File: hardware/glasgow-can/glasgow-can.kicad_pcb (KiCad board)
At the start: 2 copper layers, 34 parts, among them J1 Conn_02x10_Odd_Even, J2 A-DS 09 A/KG-T2S, J3 Conn_01x09_Male, J4 Conn_01x03_Male, J5 Conn_02x10_Odd_Even, J6 Conn_01x03, J7 Conn_01x02_Male, J8 Conn_01x02_Male, Q1 TLP240A, Q2 NX7002BKW, Q3 TLP240A, Q4 NX7002BKW, U1 TCAN1051, U2 TCAN1051

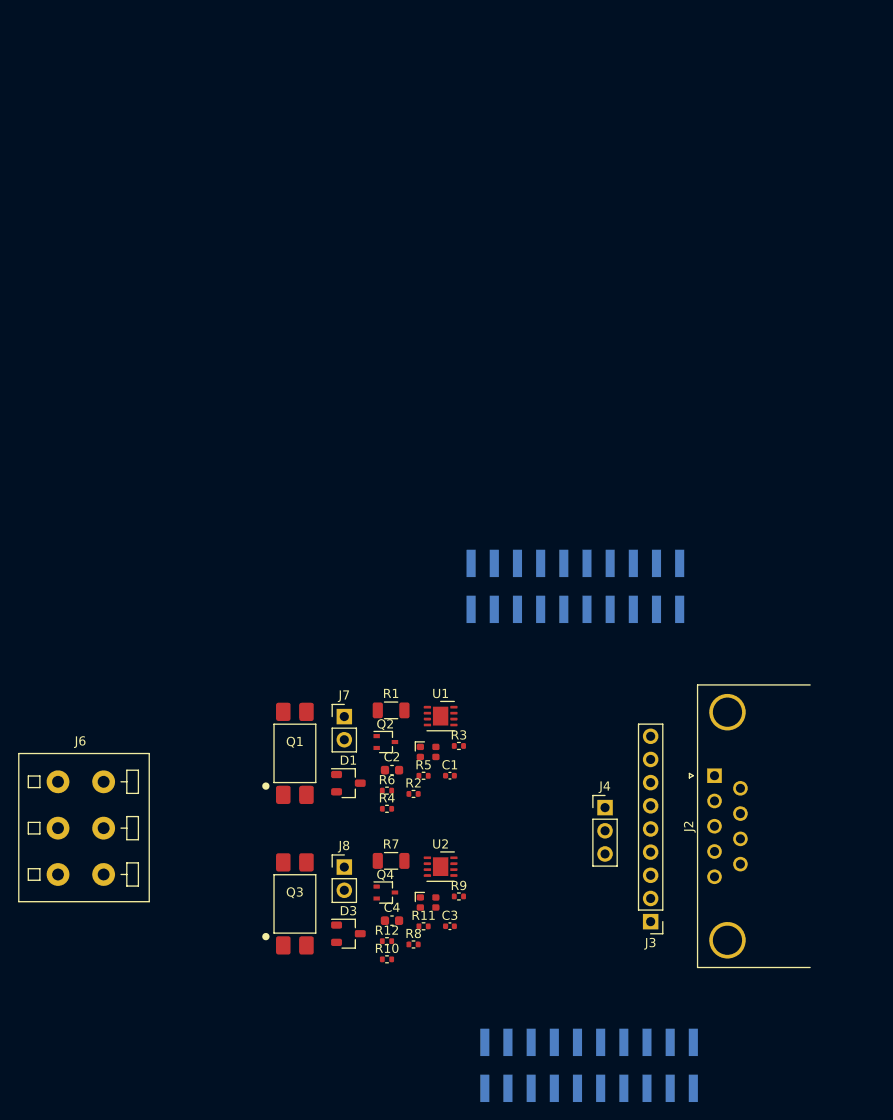
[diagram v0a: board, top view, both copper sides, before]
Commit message: schematic revised according to discussion in #1, and layout mostly complete... some TODOs remain
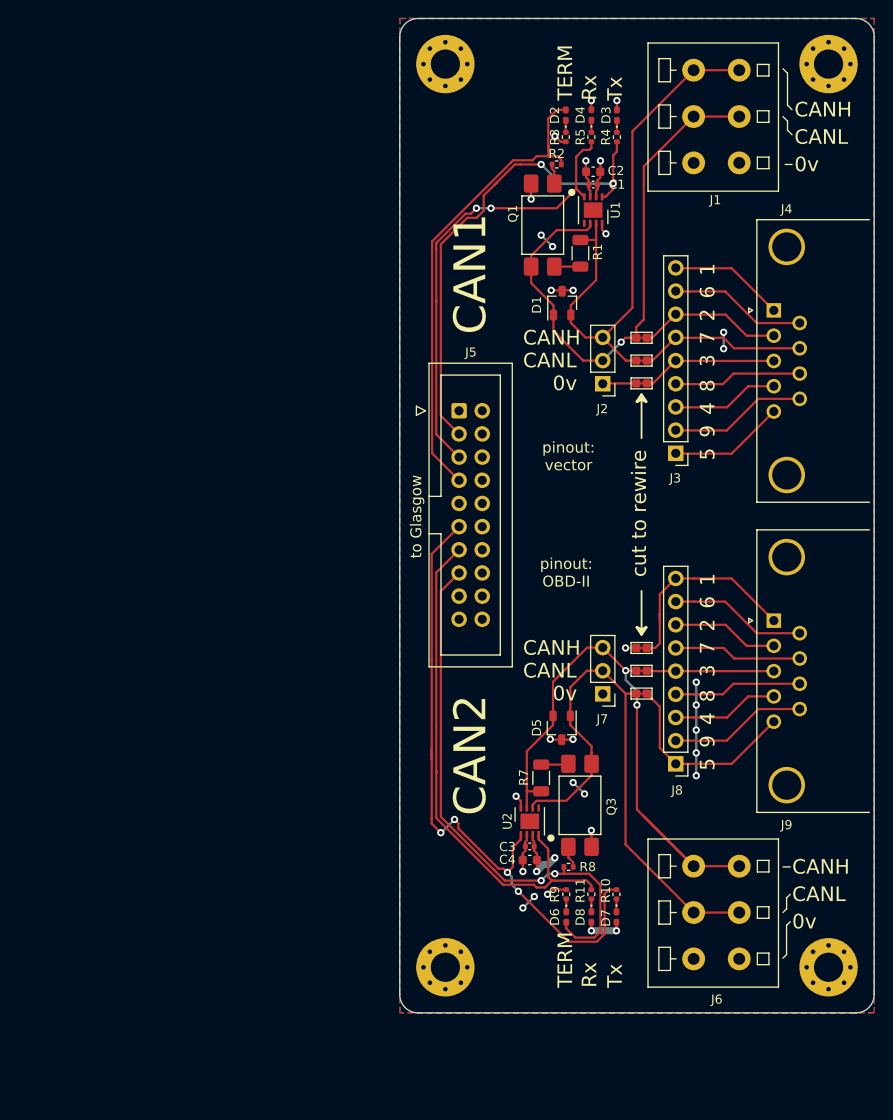
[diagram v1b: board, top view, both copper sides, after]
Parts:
- removed Q2, Q4: NX7002BKW, Package_TO_SOT_SMD:SOT-323_SC-70
- removed R12, R6: 25k, Resistor_SMD:R_0402_1005Metric
- added D5: PESD2CAN, rhais_package-smd:SOT-23, F.Cu at (171.8, 90.8)
- added D6: TJ-S1005SW4TGLC0A-A5, LED_SMD:LED_0402_1005Metric_Pad0.77x0.64mm_HandSolder, F.Cu at (172.2, 111.5)
- added D7: TJ-S1005SW4TGLC2G-A5, LED_SMD:LED_0402_1005Metric_Pad0.77x0.64mm_HandSolder, F.Cu at (177.8, 111.5)
- added D8: TJ-S1005SW4TGLC0A-A5, LED_SMD:LED_0402_1005Metric_Pad0.77x0.64mm_HandSolder, F.Cu at (175.0, 111.5)
- added H1: MountingHole_Pad, MountingHole:MountingHole_3.2mm_M3_Pad_Via, F.Cu at (159.0, 18.0)
- added H2: MountingHole_Pad, MountingHole:MountingHole_3.2mm_M3_Pad_Via, F.Cu at (201.0, 18.0)
- added H3: MountingHole_Pad, MountingHole:MountingHole_3.2mm_M3_Pad_Via, F.Cu at (159.0, 117.0)
- added H4: MountingHole_Pad, MountingHole:MountingHole_3.2mm_M3_Pad_Via, F.Cu at (201.0, 117.0)
- added J10: pkl_jumper_nc, pkl_jumpers:J_NC_0603_20, F.Cu at (180.5, 50.5)
- added J11: pkl_jumper_nc, pkl_jumpers:J_NC_0603_20, F.Cu at (180.5, 48.0)
- added J12: pkl_jumper_nc, pkl_jumpers:J_NC_0603_20, F.Cu at (180.5, 53.0)
- added J13: pkl_jumper_nc, pkl_jumpers:J_NC_0603_20, F.Cu at (180.5, 84.5)
- added J14: pkl_jumper_nc, pkl_jumpers:J_NC_0603_20, F.Cu at (180.5, 87.0)
- added J15: pkl_jumper_nc, pkl_jumpers:J_NC_0603_20, F.Cu at (180.5, 82.0)
- added J9: A-DS 09 A/KG-T2S, Connector_Dsub:DSUB-9_Female_Horizontal_P2.77x2.84mm_EdgePinOffset7.70mm_Housed_MountingHolesOffset9.12mm, F.Cu at (195.0, 79.0)
- D2, D4: value FM-B2020RGBA-HG -> TJ-S1005SW4TGLC0A-A5; footprint pkl_led:LED_TRI_2020 -> LED_SMD:LED_0402_1005Metric_Pad0.77x0.64mm_HandSolder
- D3: value PESD2CAN -> TJ-S1005SW4TGLC2G-A5; footprint rhais_package-smd:SOT-23 -> LED_SMD:LED_0402_1005Metric_Pad0.77x0.64mm_HandSolder
- J1: value Conn_02x10_Odd_Even -> 2834077-2; footprint Connector_PinSocket_2.54mm:PinSocket_2x10_P2.54mm_Vertical_SMD -> glasgow-can:TE_2834077-2; moved to F.Cu
- J2: value A-DS 09 A/KG-T2S -> Conn_01x03_Male; footprint Connector_Dsub:DSUB-9_Female_Horizontal_P2.77x2.84mm_EdgePinOffset7.70mm_Housed_MountingHolesOffset9.12mm -> Connector_PinHeader_2.54mm:PinHeader_1x03_P2.54mm_Vertical
- J4: value Conn_01x03_Male -> A-DS 09 A/KG-T2S; footprint Connector_PinHeader_2.54mm:PinHeader_1x03_P2.54mm_Vertical -> Connector_Dsub:DSUB-9_Female_Horizontal_P2.77x2.84mm_EdgePinOffset7.70mm_Housed_MountingHolesOffset9.12mm
- J5: footprint Connector_PinSocket_2.54mm:PinSocket_2x10_P2.54mm_Vertical_SMD -> Connector_IDC:IDC-Header_2x10_P2.54mm_Vertical; moved to F.Cu
- J6: value Conn_01x03 -> 2834077-2
- J7: value Conn_01x02_Male -> Conn_01x03_Male; footprint Connector_PinHeader_2.54mm:PinHeader_1x02_P2.54mm_Vertical -> Connector_PinHeader_2.54mm:PinHeader_1x03_P2.54mm_Vertical
- J8: value Conn_01x02_Male -> Conn_01x09_Male; footprint Connector_PinHeader_2.54mm:PinHeader_1x02_P2.54mm_Vertical -> Connector_PinHeader_2.54mm:PinHeader_1x09_P2.54mm_Vertical
- moved D3 94.4 mm to (177.8, 23.6), turned to 90 degrees
- moved D4 88.2 mm to (175.0, 23.6), turned to 90 degrees
- moved R4 77.8 mm to (177.8, 26.0), turned to 270 degrees
- moved J5 73.2 mm to (160.5, 56.0), turned to 0 degrees
- moved R5 72.4 mm to (175.0, 26.0), turned to 270 degrees
- moved D2 71.4 mm to (172.2, 23.6), turned to 90 degrees
- moved R2 70.8 mm to (171.2, 29.0)
- moved J6 70.4 mm to (188.8, 111.0), turned to 90 degrees
- moved C2 69.2 mm to (175.2, 29.8)
- moved R3 67.8 mm to (172.2, 26.0), turned to 270 degrees
- moved C1 66.7 mm to (175.2, 31.2)
- moved Q1 64.0 mm to (169.7, 35.6), turned to 180 degrees
- moved U1 57.9 mm to (175.2, 34.0), turned to 270 degrees
- moved D1 57.6 mm to (171.8, 44.2), turned to 90 degrees
- moved J4 57.6 mm to (195.0, 45.0), turned to 90 degrees
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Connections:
- C1 pad 1: /CAN1_+5V -> /+5V
- C2 pad 1: /CAN1_+5V -> /+5V
- C3 pad 1: /CAN2_+5V -> /+5V
- C4 pad 1: /CAN2_+5V -> /+5V
- D1 pad 1: /CAN1_H -> /CAN1_L
- D1 pad 2: /CAN1_L -> /CAN1_H
- D2 pad 2: Net-(D2-Pad2) -> /CAN1_TERM
- D3 pad 1: /CAN2_H -> Net-(D3-Pad1)
- D3 pad 2: /CAN2_L -> /+5V
- D4 pad 2: Net-(D4-Pad2) -> /+5V
- J1 pad 1: Net-(J1-Pad1) -> 0V
- J1 pad 2: /CAN1_+5V -> /CAN1_L
- J1 pad 3: /CAN1_TxD -> /CAN1_H
- J1 pad 5: /CAN1_RxD -> /CAN1_L
- J1 pad 6: 0V -> /CAN1_H
- J2 pad 1: Net-(J2-Pad1) -> 0V
- J2 pad 2: Net-(J2-Pad2) -> /CAN1_L
- J2 pad 3: Net-(J2-Pad3) -> /CAN1_H
- J3 pad 1: Net-(J2-Pad5) -> Net-(J3-Pad1)
- J3 pad 2: Net-(J2-Pad9) -> Net-(J3-Pad2)
- J3 pad 3: Net-(J2-Pad4) -> Net-(J3-Pad3)
- J3 pad 4: Net-(J2-Pad8) -> Net-(J3-Pad4)
- J3 pad 5: Net-(J2-Pad3) -> Net-(J12-Pad2)
- J3 pad 6: Net-(J2-Pad7) -> Net-(J10-Pad2)
- J3 pad 7: Net-(J2-Pad2) -> Net-(J11-Pad2)
- J3 pad 8: Net-(J2-Pad6) -> Net-(J3-Pad8)
- J3 pad 9: Net-(J2-Pad1) -> Net-(J3-Pad9)
- J4 pad 1: /CAN1_H -> Net-(J3-Pad9)
- J4 pad 2: /CAN1_L -> Net-(J11-Pad2)
- J4 pad 3: 0V -> Net-(J12-Pad2)
- J5 pad 11: /CAN2_TxLED -> /CAN2_TxD
- J5 pad 13: /CAN2_RxLED -> /CAN2_RxD
- J5 pad 15: Net-(J5-Pad15) -> /CAN2_TERM
- J5 pad 2: /CAN2_+5V -> /+5V
- J5 pad 3: /CAN2_TxD -> /CAN1_TxD
- J5 pad 5: /CAN2_RxD -> /CAN1_RxD
- J5 pad 7: /CAN2_S -> /CAN1_TERM
- J5 pad 9: /CAN2_TERM -> Net-(J5-Pad9)
- J6 pad 4: (no net) -> 0V
- J6 pad 5: (no net) -> /CAN2_L
- J6 pad 6: (no net) -> /CAN2_H
- J7 pad 1: /CAN1_L -> 0V
- J7 pad 2: 0V -> /CAN2_L
- J8 pad 1: /CAN2_L -> Net-(J14-Pad2)
- J8 pad 2: 0V -> Net-(J8-Pad2)
- R10 pad 1: Net-(D4-Pad4) -> Net-(D7-Pad1)
- R10 pad 2: /CAN2_TxLED -> /CAN2_TxD
- R11 pad 1: Net-(D4-Pad2) -> Net-(D8-Pad1)
- R11 pad 2: /CAN2_RxLED -> /CAN2_RxD
- R3 pad 2: Net-(Q2-Pad3) -> 0V
- R4 pad 1: Net-(D2-Pad4) -> Net-(D3-Pad1)
- R4 pad 2: /CAN1_TxLED -> /CAN1_TxD
- R5 pad 1: Net-(D2-Pad2) -> Net-(D4-Pad1)
- R5 pad 2: /CAN1_RxLED -> /CAN1_RxD
- R9 pad 1: Net-(D4-Pad1) -> Net-(D6-Pad1)
- R9 pad 2: Net-(Q4-Pad3) -> 0V
- U1 pad 3: /CAN1_+5V -> /+5V
- U1 pad 8: /CAN1_S -> 0V
- U2 pad 3: /CAN2_+5V -> /+5V
- U2 pad 8: /CAN2_S -> 0V
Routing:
- net /CAN2_TxD: track 0.00 -> 72.5 mm, vias 0 -> 4
- net /CAN2_H: track 0.00 -> 65.6 mm, vias 0 -> 2
- net /CAN1_H: track 0.00 -> 61.1 mm
- net /CAN1_L: track 0.00 -> 60.8 mm, vias 0 -> 1
- net /CAN2_L: track 0.00 -> 60.2 mm
- net /CAN2_TERM: track 0.00 -> 60.1 mm, vias 0 -> 2
- net /CAN2_RxD: track 0.00 -> 57.5 mm
- net /CAN1_TxD: track 0.00 -> 53.2 mm, vias 0 -> 2
- net /CAN1_TERM: track 0.00 -> 53.1 mm
- net /CAN1_RxD: track 0.00 -> 49.9 mm, vias 0 -> 2
- net /+5V: track 0.00 -> 35.0 mm, vias 0 -> 20
- net 0V: track 0.00 -> 29.1 mm, vias 0 -> 13
- net Net-(J15-Pad2): track 0.00 -> 22.9 mm
- net Net-(J14-Pad2): track 0.00 -> 21.7 mm
- net Net-(J10-Pad2): track 0.00 -> 18.3 mm
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- added copper zone on F.Cu, net /+5V
- added copper zone on B.Cu, net 0V
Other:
- board outline added: 52 x 109 mm
- board text added: "(0v)"
- board text added: "(Hi)"
- board text added: "(Lo)"
- board text added: "0v"
- board text added: "1"
- board text added: "2"
- board text added: "3"
- board text added: "4"
- board text added: "5"
- board text added: "6"
- board text added: "7"
- board text added: "8"
- board text added: "9"
- board text added: "CAN1"
- board text added: "CAN2"
- board text added: "CANH"
- board text added: "CANL"
- board text added: "Glasgow 2x CAN Add-On"
- board text added: "Rx"
- board text added: "TERM"
- board text added: "Tx"
- board text added: "cut to rewire"
- board text added: "default pinout: OBD-II cable"
- board text added: "default pinout: bosch / vector"
- board text added: "designed by: Attie Grande"
- board text added: "pinout: OBD-II"
- board text added: "pinout: vector"
- board text added: "to Glasgow"

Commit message: fix DE-9 footprint, spruce up schematic and layout
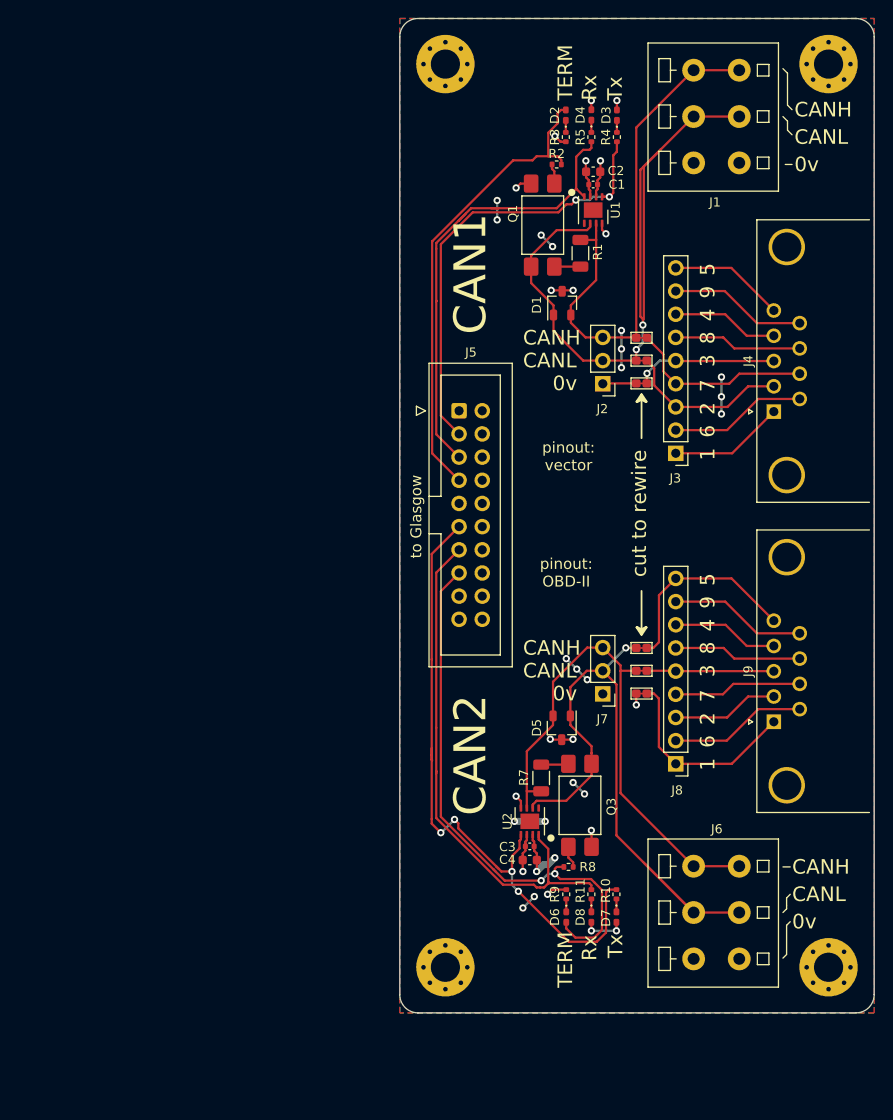
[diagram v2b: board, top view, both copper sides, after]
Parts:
- J4, J9: footprint Connector_Dsub:DSUB-9_Female_Horizontal_P2.77x2.84mm_EdgePinOffset7.70mm_Housed_MountingHolesOffset9.12mm -> Connector_Dsub:DSUB-9_Male_Horizontal_P2.77x2.84mm_EdgePinOffset7.70mm_Housed_MountingHolesOffset9.12mm
- moved J4 11.1 mm to (195.0, 56.1)
- moved J9 11.1 mm to (195.0, 90.1)
- moved J14 5.00 mm to (180.5, 82.0)
- moved J15 5.00 mm to (180.5, 87.0)
- moved J10 2.50 mm to (180.5, 48.0)
- moved J11 2.50 mm to (180.5, 50.5)
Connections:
- J3 pad 3: Net-(J3-Pad3) -> Net-(J11-Pad2)
- J3 pad 4: Net-(J3-Pad4) -> Net-(J10-Pad2)
- J3 pad 6: Net-(J10-Pad2) -> Net-(J3-Pad6)
- J3 pad 7: Net-(J11-Pad2) -> Net-(J3-Pad7)
- J4 pad 1: Net-(J3-Pad9) -> Net-(J3-Pad1)
- J4 pad 4: Net-(J3-Pad3) -> Net-(J3-Pad7)
- J4 pad 5: Net-(J3-Pad1) -> Net-(J3-Pad9)
- J4 pad 6: Net-(J3-Pad8) -> Net-(J3-Pad2)
- J4 pad 8: Net-(J3-Pad4) -> Net-(J3-Pad6)
- J4 pad 9: Net-(J3-Pad2) -> Net-(J3-Pad8)
- J8 pad 1: Net-(J14-Pad2) -> Net-(J15-Pad2)
- J8 pad 9: Net-(J15-Pad2) -> Net-(J14-Pad2)
- J9 pad 2: Net-(J8-Pad7) -> Net-(J8-Pad3)
- J9 pad 4: Net-(J8-Pad3) -> Net-(J8-Pad7)
- J9 pad 6: Net-(J8-Pad8) -> Net-(J8-Pad2)
- J9 pad 7: Net-(J8-Pad6) -> Net-(J8-Pad4)
- J9 pad 8: Net-(J8-Pad4) -> Net-(J8-Pad6)
- J9 pad 9: Net-(J8-Pad2) -> Net-(J8-Pad8)
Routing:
- net /CAN1_L: track 60.8 -> 83.7 mm, vias 1 -> 2
- net Net-(J3-Pad6): track 0.00 -> 14.1 mm
- net Net-(J3-Pad4): track 14.1 -> 0.00 mm
- net Net-(J3-Pad7): track 0.00 -> 11.7 mm
- net Net-(J3-Pad3): track 11.7 -> 0.00 mm
- net /CAN2_L: track 60.2 -> 71.1 mm, vias 0 -> 1
- net /CAN2_H: track 65.6 -> 58.5 mm, vias 2 -> 0
- net /+5V: track 35.0 -> 39.8 mm, vias 20 -> 26
- net /CAN1_TxD: track 53.2 -> 49.8 mm
- net /CAN1_H: track 61.1 -> 58.6 mm
- net Net-(J11-Pad2): track 16.0 -> 18.1 mm
- net Net-(J10-Pad2): track 18.3 -> 20.4 mm
- net /CAN1_RxD: track 49.9 -> 51.8 mm, vias 2 -> 0
- net /CAN2_TERM: track 60.1 -> 61.1 mm
- net /CAN1_TERM: track 53.1 -> 52.3 mm
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
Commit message: fixup README, and other misc changes
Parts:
- added LOGO1: Logo_Open_Hardware_Large, Symbol:OSHW-Logo2_7.3x6mm_SilkScreen, B.Cu at (200.8, 109.2)
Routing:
- net /+5V: track 39.8 -> 43.2 mm, vias 26 -> 28
- net /CAN2_TxD: track 72.9 -> 74.8 mm, vias 4 -> 2
- net 0V: track 29.3 -> 28.8 mm
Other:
- board text added: "2020-12-04"
- board text added: "Attie Grande"
- board text added: "date:"
- board text added: "designed by:"
- board text removed: "designed by: Attie Grande"

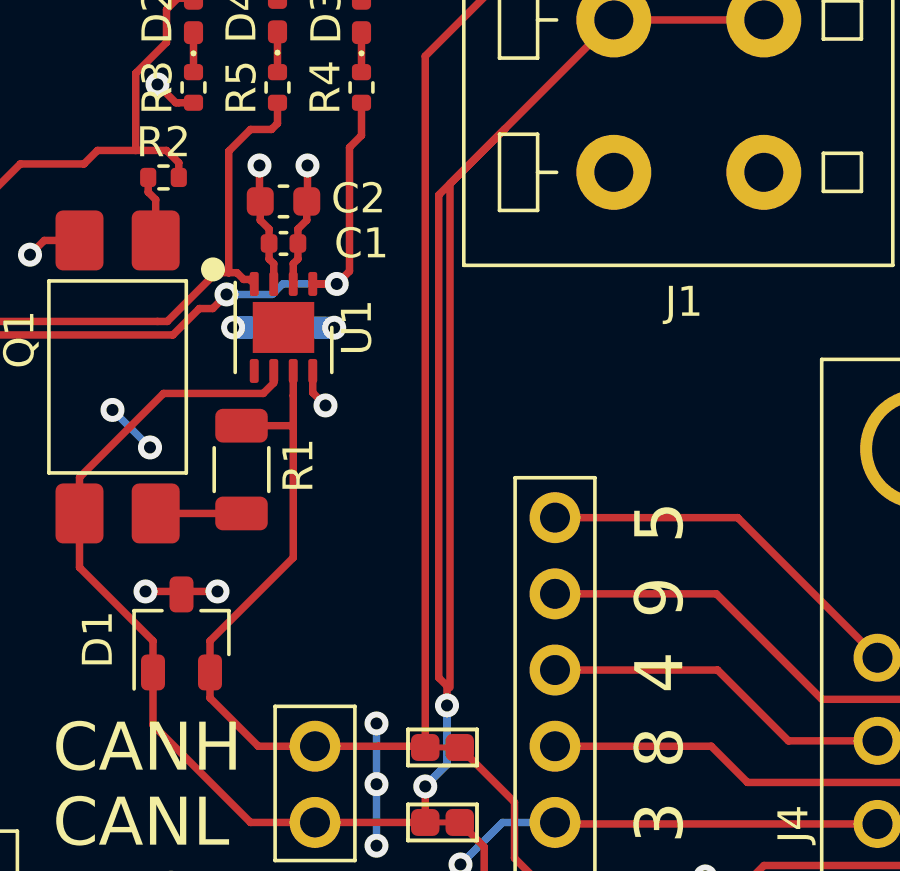
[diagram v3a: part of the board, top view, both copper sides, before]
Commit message: remove stray trace
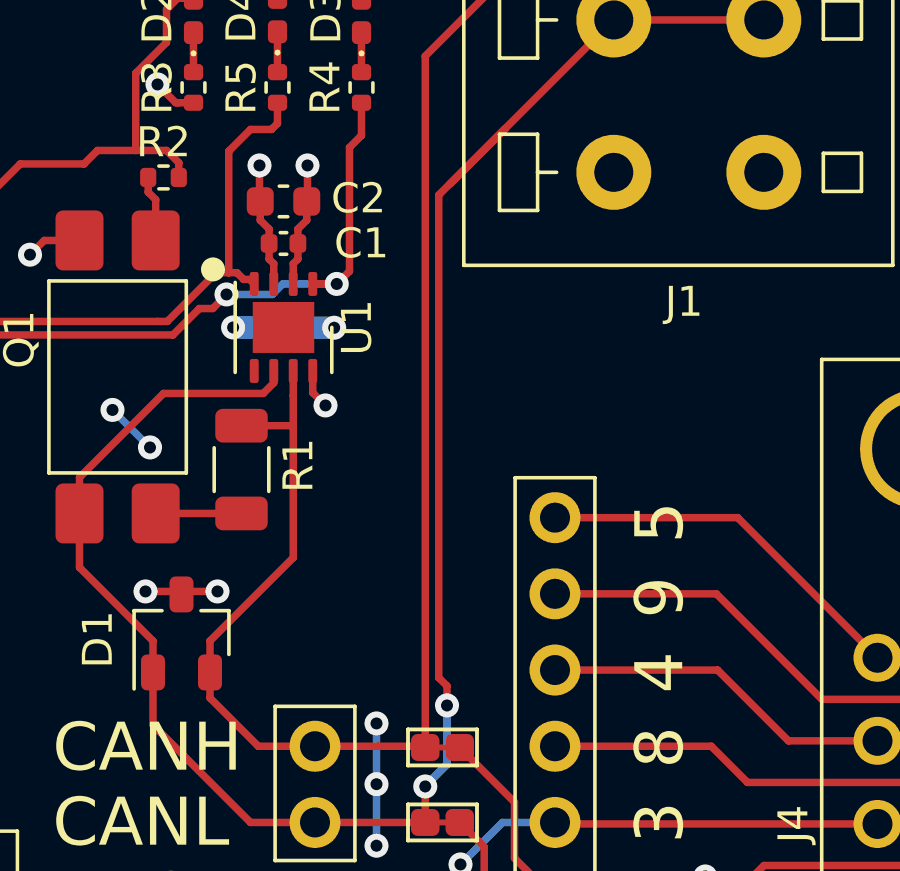
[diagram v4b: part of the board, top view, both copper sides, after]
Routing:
- net /CAN1_L: track 83.7 -> 66.9 mm

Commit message: minor tweaks
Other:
- board text added: "2020-12-19"
- board text removed: "2020-12-04"
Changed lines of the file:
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@@
   (general
     (thickness 1.6)
-    (drawings 135)
+    (drawings 137)
     (tracks 412)
     (zones 0)
@@
   )
   (page A4)
+  (title_block
+    (title "Glasgow CAN")
+    (date 2020-12-19)
+    (rev r0)
+    (comment 4 "Designed by: Attie Grande")
+  )
   (layers
     (0 F.Cu signal)
@@
     (visible_elements 7FFFFFFF)
     (pcbplotparams
-      (layerselection 0x010fc_ffffffff)
+      (layerselection 0x011fc_ffffffff)
       (usegerberextensions false)
       (usegerberattributes true)
@@
       (plotinvisibletext false)
       (padsonsilk false)
-      (subtractmaskfromsilk false)
+      (subtractmaskfromsilk true)
       (outputformat 1)
       (mirror false)
-      (drillshape 1)
+      (drillshape 0)
       (scaleselection 1)
-      (outputdirectory ""))
+      (outputdirectory "2020-12-19/"))
   )
   (net 0 "")
@@
       (effects (font (size 0.8 0.8) (thickness 0.12)))
     )
-    (pad 2 smd roundrect (at 1.4625 0 270) (size 1.125 1.75) (layers F.Cu F.Paste F.Mask) (roundrect_rratio 0.222222)
+    (pad 2 smd roundrect (at 1.4625 0 270) (size 1.125 1.75) (layers F.Cu F.Paste F.Mask) (roundrect_rratio 0.2222204444444444)
       (net 9 /CAN2_H))
-    (pad 1 smd roundrect (at -1.4625 0 270) (size 1.125 1.75) (layers F.Cu F.Paste F.Mask) (roundrect_rratio 0.222222)
+    (pad 1 smd roundrect (at -1.4625 0 270) (size 1.125 1.75) (layers F.Cu F.Paste F.Mask) (roundrect_rratio 0.2222204444444444)
       (net 36 "Net-(Q3-Pad4)"))
     (model ${KISYS3DMOD}/Resistor_SMD.3dshapes/R_1206_3216Metric.wrl
@@
       (effects (font (size 0.8 0.8) (thickness 0.12)))
     )
-    (pad 2 smd roundrect (at 1.4625 0 90) (size 1.125 1.75) (layers F.Cu F.Paste F.Mask) (roundrect_rratio 0.222222)
+    (pad 2 smd roundrect (at 1.4625 0 90) (size 1.125 1.75) (layers F.Cu F.Paste F.Mask) (roundrect_rratio 0.2222204444444444)
       (net 3 /CAN1_H))
-    (pad 1 smd roundrect (at -1.4625 0 90) (size 1.125 1.75) (layers F.Cu F.Paste F.Mask) (roundrect_rratio 0.222222)
+    (pad 1 smd roundrect (at -1.4625 0 90) (size 1.125 1.75) (layers F.Cu F.Paste F.Mask) (roundrect_rratio 0.2222204444444444)
       (net 34 "Net-(Q1-Pad4)"))
     (model ${KISYS3DMOD}/Resistor_SMD.3dshapes/R_1206_3216Metric.wrl
@@
     (pad 3 thru_hole circle (at 0 2.54) (size 1.7 1.7) (drill 1) (layers *.Cu *.Mask)
       (net 26 /CAN1_TxD))
-    (pad 1 thru_hole roundrect (at 0 0) (size 1.7 1.7) (drill 1) (layers *.Cu *.Mask) (roundrect_rratio 0.147059)
+    (pad 1 thru_hole roundrect (at 0 0) (size 1.7 1.7) (drill 1) (layers *.Cu *.Mask) (roundrect_rratio 0.1470588235294118)
       (net 27 "Net-(J5-Pad1)"))
     (model ${KISYS3DMOD}/Connector_IDC.3dshapes/IDC-Header_2x10_P2.54mm_Vertical.wrl
@@
     )
   )
+  (dimension 109 (width 0.15) (layer Dwgs.User)
+    (gr_text "109.000 mm" (at 150.7 67.5 90) (layer Dwgs.User)
+      (effects (font (size 1 1) (thickness 0.15)))
+    )
+    (feature1 (pts (xy 156 13) (xy 151.413579 13)))
+    (feature2 (pts (xy 156 122) (xy 151.413579 122)))
+    (crossbar (pts (xy 152 122) (xy 152 13)))
+    (arrow1a (pts (xy 152 13) (xy 152.586421 14.126504)))
+    (arrow1b (pts (xy 152 13) (xy 151.413579 14.126504)))
+    (arrow2a (pts (xy 152 122) (xy 152.586421 120.873496)))
+    (arrow2b (pts (xy 152 122) (xy 151.413579 120.873496)))
+  )
+  (dimension 52 (width 0.15) (layer Dwgs.User)
+    (gr_text "52.000 mm" (at 180 125.299999) (layer Dwgs.User)
+      (effects (font (size 1 1) (thickness 0.15)))
+    )
+    (feature1 (pts (xy 206 120) (xy 206 124.58642)))
+    (feature2 (pts (xy 154 120) (xy 154 124.58642)))
+    (crossbar (pts (xy 154 123.999999) (xy 206 123.999999)))
+    (arrow1a (pts (xy 206 123.999999) (xy 204.873496 124.58642)))
+    (arrow1b (pts (xy 206 123.999999) (xy 204.873496 123.413578)))
+    (arrow2a (pts (xy 154 123.999999) (xy 155.126504 124.58642)))
+    (arrow2b (pts (xy 154 123.999999) (xy 155.126504 123.413578)))
+  )
   (gr_text "Attie Grande" (at 160.4 38.6 90) (layer B.SilkS)
     (effects (font (size 1.4 1.4) (thickness 0.15)) (justify left mirror))
   )
-  (gr_text 2020-12-04 (at 163 38.6 90) (layer B.SilkS)
+  (gr_text 2020-12-19 (at 163 38.6 90) (layer B.SilkS)
     (effects (font (size 1.4 1.4) (thickness 0.15)) (justify left mirror))
   )
